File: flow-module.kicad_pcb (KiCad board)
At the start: 2 copper layers, 60 x 47.2 mm, 22 parts, among them P1 12V, P2 tL298P, P3 tLMD..., P4 fL298P, P5 fLMD...

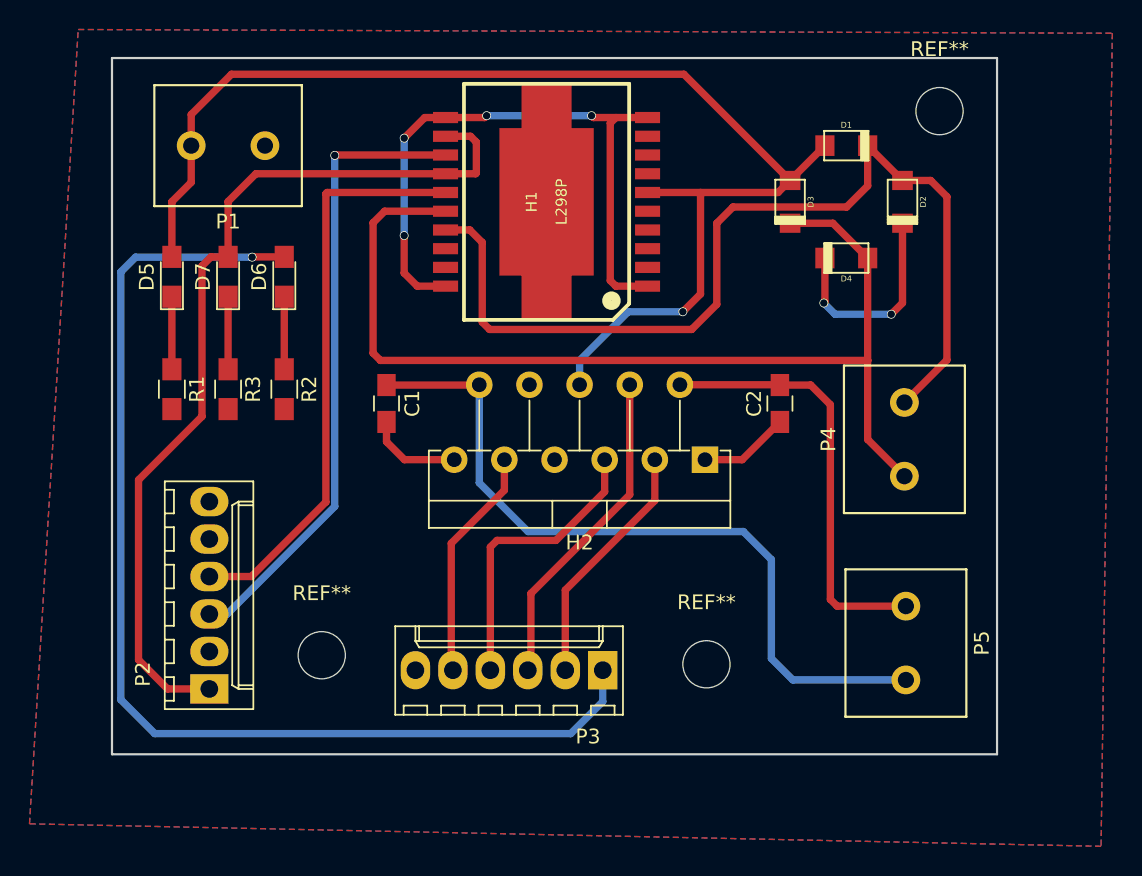
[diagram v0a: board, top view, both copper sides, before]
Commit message: Add more vias between ground planes.
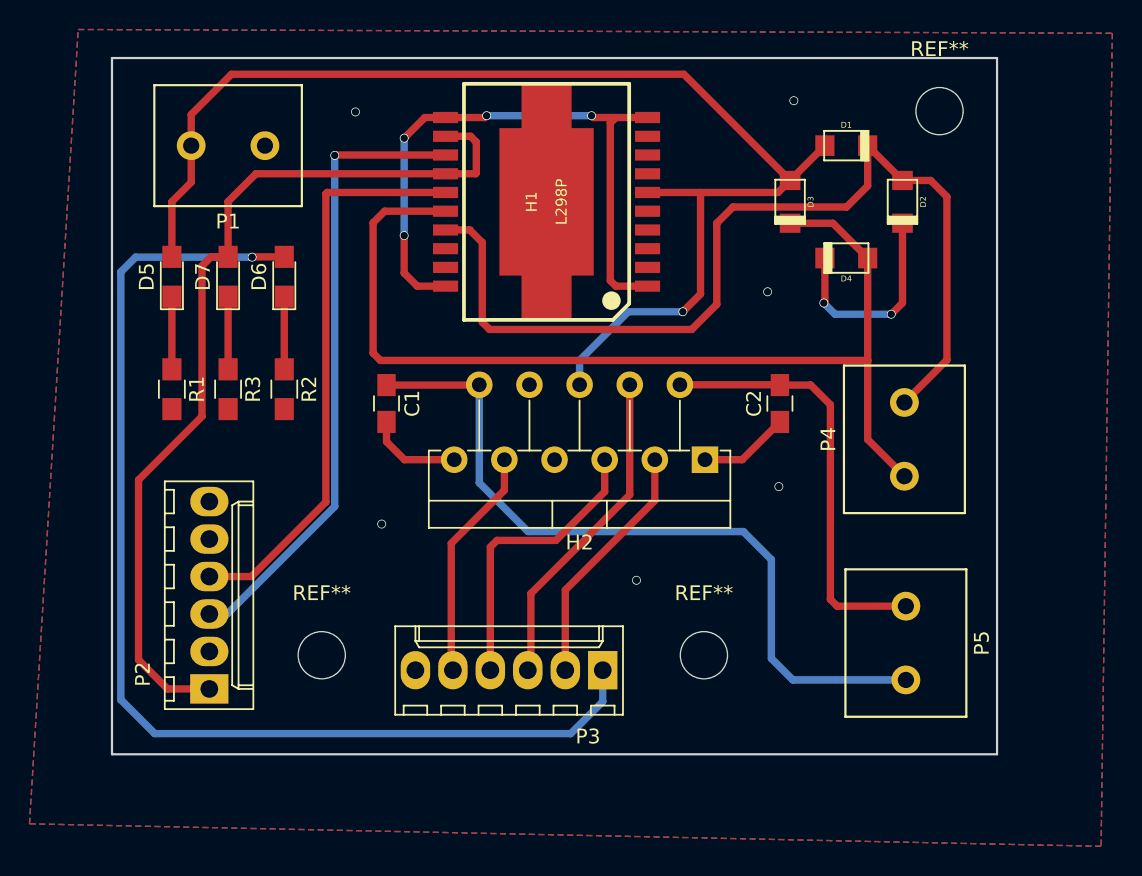
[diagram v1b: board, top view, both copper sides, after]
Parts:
- moved REF** 0.64 mm to (109.7, 62.5)
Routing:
- net Earth: vias 6 -> 12
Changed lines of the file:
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@@
     (thickness 1.6)
     (drawings 4)
-    (tracks 147)
+    (tracks 153)
     (zones 0)
     (modules 22)
@@
   )
   (module Mounting_Holes:MountingHole_3.2mm_M3 (layer F.Cu)
-    (at 109.9 63.1)
+    (at 109.728 62.484)
     (descr "Mounting Hole 3.2mm, no annular, M3")
     (tags "mounting hole 3.2mm no annular m3")
@@
   (segment (start 73.66 31.74) (end 73.66 35.48) (width 0.5) (layer F.Cu) (net 6))
   (segment (start 74.97 30.43) (end 73.66 31.74) (width 0.5) (layer F.Cu) (net 6))
+  (via (at 115.824 24.892) (size 0.6) (drill 0.5) (layers F.Cu B.Cu) (net 7))
+  (via (at 86.106 25.654) (size 0.6) (drill 0.5) (layers F.Cu B.Cu) (net 7))
+  (via (at 87.884 53.594) (size 0.6) (drill 0.5) (layers F.Cu B.Cu) (net 7))
+  (via (at 114.046 37.846) (size 0.6) (drill 0.5) (layers F.Cu B.Cu) (net 7))
+  (via (at 114.808 51.054) (size 0.6) (drill 0.5) (layers F.Cu B.Cu) (net 7))
+  (via (at 105.156 57.404) (size 0.6) (drill 0.5) (layers F.Cu B.Cu) (net 7))
   (segment (start 117.92966 35.56) (end 117.92966 38.53434) (width 0.5) (layer F.Cu) (net 7))
   (segment (start 123.19 38.608) (end 123.19 33.20034) (width 0.5) (layer F.Cu) (net 7))

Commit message: Files for PCB production (added for reference).
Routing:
- net Earth: vias 12 -> 6
- net (no net): vias 0 -> 6
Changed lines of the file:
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@@
     (links 43)
     (no_connects 0)
-    (area 69.524999 21.924999 129.675001 69.275001)
+    (area 64.008 20.066 137.414001 75.438001)
     (thickness 1.6)
     (drawings 4)
@@
     (pad_to_mask_clearance 0.2)
     (aux_axis_origin 0 0)
-    (visible_elements FFFFFF7F)
+    (visible_elements 7FFFFFFF)
     (pcbplotparams
-      (layerselection 0x00030_80000001)
+      (layerselection 0x01000_80000001)
       (usegerberextensions false)
       (excludeedgelayer true)
@@
       (padsonsilk false)
       (subtractmaskfromsilk false)
-      (outputformat 1)
+      (outputformat 4)
       (mirror false)
-      (drillshape 1)
+      (drillshape 0)
       (scaleselection 1)
       (outputdirectory ""))
@@
   (gr_line (start 129.6 22) (end 129.6 69.2) (angle 90) (layer Edge.Cuts) (width 0.15))
   (gr_line (start 69.6 22) (end 129.6 22) (angle 90) (layer Edge.Cuts) (width 0.15))
+  (via (at 115.824 24.892) (size 0.6) (drill 0.5) (layers F.Cu B.Cu) (net 0))
+  (via (at 86.106 25.654) (size 0.6) (drill 0.5) (layers F.Cu B.Cu) (net 0))
+  (via (at 87.884 53.594) (size 0.6) (drill 0.5) (layers F.Cu B.Cu) (net 0))
+  (via (at 114.046 37.846) (size 0.6) (drill 0.5) (layers F.Cu B.Cu) (net 0))
+  (via (at 114.808 51.054) (size 0.6) (drill 0.5) (layers F.Cu B.Cu) (net 0))
+  (via (at 105.156 57.404) (size 0.6) (drill 0.5) (layers F.Cu B.Cu) (net 0))
   (segment (start 94.5 44.15) (end 94.5 50.8) (width 0.5) (layer B.Cu) (net 1))
   (segment (start 115.76 64.16) (end 123.42 64.16) (width 0.5) (layer B.Cu) (net 1))
@@
   (segment (start 73.66 31.74) (end 73.66 35.48) (width 0.5) (layer F.Cu) (net 6))
   (segment (start 74.97 30.43) (end 73.66 31.74) (width 0.5) (layer F.Cu) (net 6))
-  (via (at 115.824 24.892) (size 0.6) (drill 0.5) (layers F.Cu B.Cu) (net 7))
-  (via (at 86.106 25.654) (size 0.6) (drill 0.5) (layers F.Cu B.Cu) (net 7))
-  (via (at 87.884 53.594) (size 0.6) (drill 0.5) (layers F.Cu B.Cu) (net 7))
-  (via (at 114.046 37.846) (size 0.6) (drill 0.5) (layers F.Cu B.Cu) (net 7))
-  (via (at 114.808 51.054) (size 0.6) (drill 0.5) (layers F.Cu B.Cu) (net 7))
-  (via (at 105.156 57.404) (size 0.6) (drill 0.5) (layers F.Cu B.Cu) (net 7))
   (segment (start 117.92966 35.56) (end 117.92966 38.53434) (width 0.5) (layer F.Cu) (net 7))
   (segment (start 123.19 38.608) (end 123.19 33.20034) (width 0.5) (layer F.Cu) (net 7))
